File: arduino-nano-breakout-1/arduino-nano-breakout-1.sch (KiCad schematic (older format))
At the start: 4 parts, among them J1 PJ-002A, J2 Conn_01x03_Male, J4 Conn_01x08_Male

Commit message: move
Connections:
- net at A1.27 (+5V), J2.1 (Pin_1): no longer J4.2 (Pin_2)
- net at J1.1, J2.2 (Pin_2): now also J4.2 (Pin_2)
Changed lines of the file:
@@
 	6650 3300 6750 3300
 Wire Wire Line
-	5250 2100 5250 2650
-Wire Wire Line
-	6400 3900 6400 2650
-Wire Wire Line
-	6400 2650 5250 2650
-Wire Wire Line
 	6400 3900 6750 3900
-Connection ~ 5250 2650
-Wire Wire Line
-	5250 2650 5250 2800
 Wire Wire Line
 	6400 4000 6400 4800
@@
 Wire Wire Line
 	6650 3800 6750 3800
+Wire Wire Line
+	5250 2100 5250 2800
+Wire Wire Line
+	6400 3900 6400 2200
+Wire Wire Line
+	6400 2200 5150 2200
+Connection ~ 5150 2200
 $EndSCHEMATC

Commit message: final piece?
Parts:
- added JP1, JP2, JP3, JP4: SolderJumper_3_Open, Jumper:SolderJumper-3_P1.3mm_Open_Pad1.0x1.5mm, symbol Jumper:SolderJumper_3_Open
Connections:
- net GND: now also J4.7 (Pin_7); no longer J4.1 (Pin_1)
- net IO10: now also J4.6 (Pin_6); no longer J4.8 (Pin_8)
- net IO2: now also JP1.3 (B); no longer J4.3 (Pin_3)
- net IO3: now also JP2.3 (B); no longer J4.4 (Pin_4)
- net IO5: now also JP3.3 (B); no longer J4.5 (Pin_5)
- net IO6: now also JP4.3 (B); no longer J4.6 (Pin_6)
- net IO9: now also J4.5 (Pin_5); no longer J4.7 (Pin_7)
- net at A1.21 (A2): now also JP1.1 (A)
- net at A1.22 (A3): now also JP2.1 (A)
- net at A1.24 (A5): now also JP3.1 (A)
- net at A1.25 (A6): now also JP4.1 (A)
- net at J1.1, J2.2 (Pin_2): now also J4.8 (Pin_8); no longer J4.2 (Pin_2)
- new net: J4.1 (Pin_1), JP1.2 (C)
- new net: J4.2 (Pin_2), JP2.2 (C)
- new net: J4.3 (Pin_3), JP3.2 (C)
- new net: J4.4 (Pin_4), JP4.2 (C)
- no-connect marks 1 -> 17
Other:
- moved on the sheet: J4
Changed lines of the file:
@@
 $EndDescr
-$Comp
-L MCU_Module:Arduino_Nano_v3.x A1
-U 1 1 5BF57DB9
-P 5050 3800
-F 0 "A1" H 5050 2714 50  0000 C CNN
-F 1 "Arduino_Nano_v3.x" H 5050 2623 50  0000 C CNN
-F 2 "Module:Arduino_Nano" H 5200 2850 50  0001 L CNN
-F 3 "http://www.mouser.com/pdfdocs/Gravitech_Arduino_Nano3_0.pdf" H 5050 2800 50  0001 C CNN
-	1    5050 3800
-	1    0    0    -1
-$EndComp
 $Comp
 L SS_connectors:PJ-002A J1
@@
 L power:GND #PWR0101
 U 1 1 5BF59927
-P 5200 5150
-F 0 "#PWR0101" H 5200 4900 50  0001 C CNN
-F 1 "GND" H 5205 4977 50  0000 C CNN
-F 2 "" H 5200 5150 50  0001 C CNN
-F 3 "" H 5200 5150 50  0001 C CNN
-	1    5200 5150
-	1    0    0    -1
-$EndComp
-$Comp
-L power:GND #PWR0102
-U 1 1 5BF59956
-P 5000 5150
-F 0 "#PWR0102" H 5000 4900 50  0001 C CNN
-F 1 "GND" H 5005 4977 50  0000 C CNN
-F 2 "" H 5000 5150 50  0001 C CNN
-F 3 "" H 5000 5150 50  0001 C CNN
-	1    5000 5150
-	1    0    0    -1
-$EndComp
-Wire Wire Line
-	5200 4800 5200 5150
-Wire Wire Line
-	5000 4800 5000 5150
-Wire Wire Line
-	5200 4800 5150 4800
-Wire Wire Line
-	5050 4800 5000 4800
+P 5150 5150
+F 0 "#PWR0101" H 5150 4900 50  0001 C CNN
+F 1 "GND" H 5155 4977 50  0000 C CNN
+F 2 "" H 5150 5150 50  0001 C CNN
+F 3 "" H 5150 5150 50  0001 C CNN
+	1    5150 5150
+	1    0    0    -1
+$EndComp
 $Comp
 L power:GND #PWR0103
@@
 Wire Wire Line
 	5050 2650 4950 2650
-Wire Wire Line
-	4950 2650 4950 2800
 $Comp
 L Connector:Conn_01x08_Male J4
 U 1 1 5BF5B051
-P 6950 3700
-F 0 "J4" H 6923 3580 50  0000 R CNN
-F 1 "Conn_01x08_Male" H 6923 3671 50  0000 R CNN
-F 2 "Connector_PinHeader_2.54mm:PinHeader_1x08_P2.54mm_Vertical" H 6950 3700 50  0001 C CNN
-F 3 "~" H 6950 3700 50  0001 C CNN
-	1    6950 3700
-	-1   0    0    1
+P 7300 3700
+F 0 "J4" H 7273 3580 50  0000 R CNN
+F 1 "Conn_01x08_Male" H 7273 3671 50  0000 R CNN
+F 2 "Connector_PinHeader_2.54mm:PinHeader_1x08_P2.54mm_Vertical" H 7300 3700 50  0001 C CNN
+F 3 "~" H 7300 3700 50  0001 C CNN
+	1    7300 3700
+	-1   0    0    -1
 $EndComp
 Text GLabel 4250 3400 0    50   Input ~ 0
@@
 Wire Wire Line
 	4400 4200 4550 4200
-Text GLabel 6650 3300 0    50   Input ~ 0
+Text GLabel 7000 3900 0    50   Input ~ 0
 IO10
-Text GLabel 6650 3400 0    50   Input ~ 0
+Text GLabel 7000 3800 0    50   Input ~ 0
 IO9
 Wire Wire Line
-	6650 3400 6750 3400
-Wire Wire Line
-	6650 3300 6750 3300
-Wire Wire Line
-	6400 3900 6750 3900
-Wire Wire Line
-	6400 4000 6400 4800
-Wire Wire Line
-	6400 4800 5200 4800
-Wire Wire Line
-	6400 4000 6750 4000
-Connection ~ 5200 4800
-Text GLabel 6650 3500 0    50   Input ~ 0
+	7000 3800 7100 3800
+Wire Wire Line
+	7000 3900 7100 3900
+Text GLabel 6500 4000 1    50   Input ~ 0
 IO6
-Text GLabel 6650 3600 0    50   Input ~ 0
+Text GLabel 6250 3900 1    50   Input ~ 0
 IO5
-Text GLabel 6650 3700 0    50   Input ~ 0
+Text GLabel 6000 3700 1    50   Input ~ 0
 IO3
-Text GLabel 6650 3800 0    50   Input ~ 0
+Text GLabel 5750 3600 1    50   Input ~ 0
 IO2
 Wire Wire Line
-	6650 3500 6750 3500
-Wire Wire Line
-	6650 3600 6750 3600
-Wire Wire Line
-	6650 3700 6750 3700
-Wire Wire Line
-	6650 3800 6750 3800
-Wire Wire Line
 	5250 2100 5250 2800
-Wire Wire Line
-	6400 3900 6400 2200
-Wire Wire Line
-	6400 2200 5150 2200
 Connection ~ 5150 2200
+Wire Wire Line
+	6750 4100 7100 4100
+$Comp
+L power:GND #PWR0104
+U 1 1 5BF6D124
+P 6950 4250
+F 0 "#PWR0104" H 6950 4000 50  0001 C CNN
+F 1 "GND" H 6955 4077 50  0000 C CNN
+F 2 "" H 6950 4250 50  0001 C CNN
+F 3 "" H 6950 4250 50  0001 C CNN
+	1    6950 4250
+	1    0    0    -1
+$EndComp
+Wire Wire Line
+	7100 4000 6950 4000
+Wire Wire Line
+	6950 4000 6950 4250
+$Comp
+L Jumper:SolderJumper_3_Open JP1
+U 1 1 5BF6F90F
+P 5750 3800
+F 0 "JP1" V 5796 3868 50  0000 L CNN
+F 1 "SolderJumper_3_Open" V 5705 3868 50  0000 L CNN
+F 2 "Jumper:SolderJumper-3_P1.3mm_Open_Pad1.0x1.5mm" H 5750 3800 50  0001 C CNN
+F 3 "~" H 5750 3800 50  0001 C CNN
+	1    5750 3800
+	0    -1   -1   0
+$EndComp
+Wire Wire Line
+	6750 2200 6750 4100
+Wire Wire Line
+	5550 4000 5750 4000
+Wire Wire Line
+	5900 3800 5900 3400
+$Comp
+L Jumper:SolderJumper_3_Open JP2
+U 1 1 5BF73B3B
+P 6000 3900
+F 0 "JP2" V 6046 3968 50  0000 L CNN
+F 1 "SolderJumper_3_Open" V 5955 3968 50  0000 L CNN
+F 2 "Jumper:SolderJumper-3_P1.3mm_Open_Pad1.0x1.5mm" H 6000 3900 50  0001 C CNN
+F 3 "~" H 6000 3900 50  0001 C CNN
+	1    6000 3900
+	0    -1   -1   0
+$EndComp
+Wire Wire Line
+	6000 4100 5550 4100
+Wire Wire Line
+	6150 3500 6150 3900
+$Comp
+L Jumper:SolderJumper_3_Open JP3
+U 1 1 5BF74A7B
+P 6250 4100
+F 0 "JP3" V 6296 4168 50  0000 L CNN
+F 1 "SolderJumper_3_Open" V 6205 4168 50  0000 L CNN
+F 2 "Jumper:SolderJumper-3_P1.3mm_Open_Pad1.0x1.5mm" H 6250 4100 50  0001 C CNN
+F 3 "~" H 6250 4100 50  0001 C CNN
+	1    6250 4100
+	0    -1   -1   0
+$EndComp
+$Comp
+L Jumper:SolderJumper_3_Open JP4
+U 1 1 5BF74AAB
+P 6500 4200
+F 0 "JP4" V 6546 4268 50  0000 L CNN
+F 1 "SolderJumper_3_Open" V 6455 4268 50  0000 L CNN
+F 2 "Jumper:SolderJumper-3_P1.3mm_Open_Pad1.0x1.5mm" H 6500 4200 50  0001 C CNN
+F 3 "~" H 6500 4200 50  0001 C CNN
+	1    6500 4200
+	0    -1   -1   0
+$EndComp
+Wire Wire Line
+	6250 4300 5550 4300
+Wire Wire Line
+	6500 4400 5550 4400
+Wire Wire Line
+	5900 3400 7100 3400
+Wire Wire Line
+	6150 3500 7100 3500
+Wire Wire Line
+	5150 2200 6750 2200
+Wire Wire Line
+	6400 3600 6400 4100
+Wire Wire Line
+	6400 3600 7100 3600
+Wire Wire Line
+	6650 3700 6650 4200
+Wire Wire Line
+	6650 3700 7100 3700
+$Comp
+L MCU_Module:Arduino_Nano_v3.x A1
+U 1 1 5BF57DB9
+P 5050 3800
+F 0 "A1" H 5050 2714 50  0000 C CNN
+F 1 "Arduino_Nano_v3.x" H 5050 2623 50  0000 C CNN
+F 2 "Module:Arduino_Nano" H 5200 2850 50  0001 L CNN
+F 3 "http://www.mouser.com/pdfdocs/Gravitech_Arduino_Nano3_0.pdf" H 5050 2800 50  0001 C CNN
+	1    5050 3800
+	1    0    0    -1
+$EndComp
+NoConn ~ 4550 3200
+NoConn ~ 4550 3300
+NoConn ~ 4550 3600
+NoConn ~ 4550 3900
+NoConn ~ 4550 4000
+NoConn ~ 4550 4300
+NoConn ~ 4550 4400
+NoConn ~ 4550 4500
+NoConn ~ 5550 4500
+NoConn ~ 5550 4200
+NoConn ~ 5550 3900
+NoConn ~ 5550 3800
+NoConn ~ 5550 3600
+NoConn ~ 5550 3300
+NoConn ~ 5550 3200
+NoConn ~ 5150 2800
+Wire Wire Line
+	4950 2650 4950 2800
+Wire Wire Line
+	5050 4800 5050 4850
+Wire Wire Line
+	5050 4850 5150 4850
+Wire Wire Line
+	5150 4850 5150 4800
+Wire Wire Line
+	5150 4850 5150 5150
+Connection ~ 5150 4850
 $EndSCHEMATC

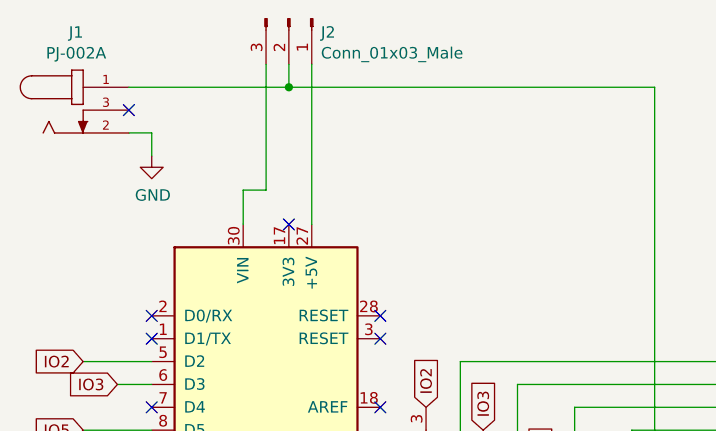
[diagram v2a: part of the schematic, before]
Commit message: VDD filtering capacitors
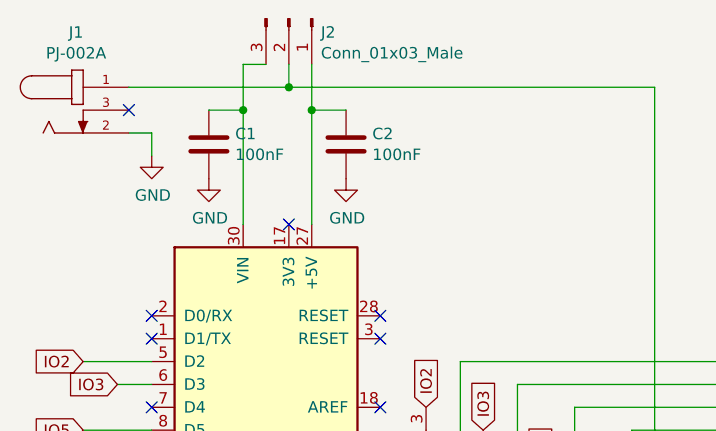
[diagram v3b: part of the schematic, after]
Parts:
- added C1, C2: 100nF, Capacitor_SMD:C_0805_2012Metric, symbol Device:C
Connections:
- net GND: now also C1.2, C2.2
- net at A1.27 (+5V), J2.1 (Pin_1): now also C2.1
- net at A1.30 (VIN), J2.3 (Pin_3): now also C1.1
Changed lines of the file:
@@
 Wire Wire Line
 	5150 2200 4450 2200
-Wire Wire Line
-	5050 2100 5050 2650
-Wire Wire Line
-	5050 2650 4950 2650
 $Comp
 L Connector:Conn_01x08_Male J4
@@
 IO2
 Wire Wire Line
-	5250 2100 5250 2800
+	5250 2100 5250 2300
 Connection ~ 5150 2200
 Wire Wire Line
@@
 NoConn ~ 5150 2800
 Wire Wire Line
-	4950 2650 4950 2800
-Wire Wire Line
 	5050 4800 5050 4850
 Wire Wire Line
@@
 	5150 4850 5150 5150
 Connection ~ 5150 4850
+$Comp
+L Device:C C2
+U 1 1 5BF6CD78
+P 5400 2450
+F 0 "C2" H 5515 2496 50  0000 L CNN
+F 1 "100nF" H 5515 2405 50  0000 L CNN
+F 2 "Capacitor_SMD:C_0805_2012Metric" H 5438 2300 50  0001 C CNN
+F 3 "~" H 5400 2450 50  0001 C CNN
+	1    5400 2450
+	1    0    0    -1
+$EndComp
+$Comp
+L Device:C C1
+U 1 1 5BF6CE4A
+P 4800 2450
+F 0 "C1" H 4915 2496 50  0000 L CNN
+F 1 "100nF" H 4915 2405 50  0000 L CNN
+F 2 "Capacitor_SMD:C_0805_2012Metric" H 4838 2300 50  0001 C CNN
+F 3 "~" H 4800 2450 50  0001 C CNN
+	1    4800 2450
+	1    0    0    -1
+$EndComp
+Wire Wire Line
+	5050 2100 4950 2100
+Wire Wire Line
+	4950 2100 4950 2300
+$Comp
+L power:GND #PWR0102
+U 1 1 5BF6DF10
+P 4800 2600
+F 0 "#PWR0102" H 4800 2350 50  0001 C CNN
+F 1 "GND" H 4805 2427 50  0000 C CNN
+F 2 "" H 4800 2600 50  0001 C CNN
+F 3 "" H 4800 2600 50  0001 C CNN
+	1    4800 2600
+	1    0    0    -1
+$EndComp
+$Comp
+L power:GND #PWR0105
+U 1 1 5BF6DF2F
+P 5400 2600
+F 0 "#PWR0105" H 5400 2350 50  0001 C CNN
+F 1 "GND" H 5405 2427 50  0000 C CNN
+F 2 "" H 5400 2600 50  0001 C CNN
+F 3 "" H 5400 2600 50  0001 C CNN
+	1    5400 2600
+	1    0    0    -1
+$EndComp
+Wire Wire Line
+	5400 2300 5250 2300
+Connection ~ 5250 2300
+Wire Wire Line
+	5250 2300 5250 2800
+Wire Wire Line
+	4950 2300 4800 2300
+Connection ~ 4950 2300
+Wire Wire Line
+	4950 2300 4950 2800
 $EndSCHEMATC
